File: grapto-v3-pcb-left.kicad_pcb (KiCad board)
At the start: 2 copper layers, 150.1 x 129.9 mm, 62 parts, among them J1 USB_C_Receptacle_USB2.0, J2 USB_C_Receptacle_USB2.0, SW1 SW_Push, SW10 SW_Push, SW11 SW_Push, SW12 SW_Push, SW13 SW_Push, SW14 SW_Push, SW15 SW_Push, SW16 SW_Push, SW17 SW_Push, SW18 SW_Push, SW19 SW_Push, SW2 SW_Push, SW20 SW_Push, SW21 SW_Push, SW22 SW_Push, SW23 SW_Push, SW24 SW_Push, SW25 SW_Push, SW26 SW_Push, SW27 SW_Push, SW28 SW_Push, SW29 SW_Push, SW3 SW_Push, SW30 SW_Push, SW4 SW_Push, SW5 SW_Push, SW6 SW_Push, SW7 SW_Push, SW8 SW_Push, SW9 SW_Push

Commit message: fixed board outline
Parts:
- moved J1 153.8 mm to (215.4, 115.1)
- moved SW25 152.5 mm to (214.7, 145.9), turned to 127.5 degrees
- moved SW30 120.0 mm to (198.5, 131.0), turned to 148 degrees
- moved J2 117.8 mm to (197.4, 115.1)
- moved SW12 113.0 mm to (82.0, 98.0), turned to 180 degrees
- moved SW18 113.0 mm to (82.0, 117.0), turned to 180 degrees
- moved SW24 113.0 mm to (82.0, 151.0), turned to 180 degrees
- moved SW6 113.0 mm to (82.0, 79.0), turned to 180 degrees
- moved D16 108.0 mm to (192.0, 324.6), turned to 180 degrees
- moved D19 108.0 mm to (192.0, 327.6), turned to 180 degrees
- moved D7 108.0 mm to (192.0, 330.5), turned to 180 degrees
- moved D18 97.9 mm to (186.9, 324.6), turned to 180 degrees
- moved D20 97.9 mm to (186.9, 327.6), turned to 180 degrees
- moved D24 97.9 mm to (186.9, 330.5), turned to 180 degrees
- moved D21 87.8 mm to (181.9, 324.6), turned to 180 degrees
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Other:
- outline, holes or cut-outs redrawn

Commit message: Routed signals.
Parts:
- added C1: .1u, Capacitor_SMD:C_0603_1608Metric_Pad1.08x0.95mm_HandSolder, B.Cu at (195.1, 139.0)
- added C10: 32p, Capacitor_SMD:C_0805_2012Metric_Pad1.18x1.45mm_HandSolder, B.Cu at (180.3, 154.0)
- added C11: 32p, Capacitor_SMD:C_0805_2012Metric_Pad1.18x1.45mm_HandSolder, B.Cu at (189.8, 155.2)
- added C12: 1u, Capacitor_SMD:C_0603_1608Metric_Pad1.08x0.95mm_HandSolder, B.Cu at (177.3, 136.1)
- added C2: .1u, Capacitor_SMD:C_0603_1608Metric_Pad1.08x0.95mm_HandSolder, B.Cu at (195.1, 143.8)
- added C3: .1u, Capacitor_SMD:C_0603_1608Metric_Pad1.08x0.95mm_HandSolder, B.Cu at (189.6, 152.5)
- added C4: .1u, Capacitor_SMD:C_0603_1608Metric_Pad1.08x0.95mm_HandSolder, B.Cu at (173.9, 146.2)
- added C5: .1u, Capacitor_SMD:C_0603_1608Metric_Pad1.08x0.95mm_HandSolder, B.Cu at (177.7, 133.9)
- added C6: .1u, Capacitor_SMD:C_0603_1608Metric_Pad1.08x0.95mm_HandSolder, B.Cu at (188.8, 132.3)
- added C7: 1u, Capacitor_SMD:C_0603_1608Metric_Pad1.08x0.95mm_HandSolder, B.Cu at (193.4, 148.8)
- added C8: .1u, Capacitor_SMD:C_0603_1608Metric_Pad1.08x0.95mm_HandSolder, B.Cu at (186.8, 132.2)
- added C9: 1u, Capacitor_SMD:C_0603_1608Metric_Pad1.08x0.95mm_HandSolder, B.Cu at (195.1, 142.2)
- added D31: LED, Diode_SMD:D_0805_2012Metric_Pad1.15x1.40mm_HandSolder, B.Cu at (209.0, 130.7)
- added F1: 200m, Fuse:Fuse_0603_1608Metric_Pad1.05x0.95mm_HandSolder, B.Cu at (192.4, 125.4)
- added R1: 22, Resistor_SMD:R_0603_1608Metric_Pad0.98x0.95mm_HandSolder, B.Cu at (198.8, 127.5)
- added R2: 1.2k, Resistor_SMD:R_0603_1608Metric_Pad0.98x0.95mm_HandSolder, B.Cu at (214.2, 133.4)
- added R3: 1.2k, Resistor_SMD:R_0603_1608Metric_Pad0.98x0.95mm_HandSolder, B.Cu at (213.2, 131.6)
- added R4: 4.7k, Resistor_SMD:R_0603_1608Metric_Pad0.98x0.95mm_HandSolder, B.Cu at (193.5, 151.7)
- added R5: 5.1k, Resistor_SMD:R_0603_1608Metric_Pad0.98x0.95mm_HandSolder, B.Cu at (195.8, 127.5)
- added R6: 5.1k, Resistor_SMD:R_0603_1608Metric_Pad0.98x0.95mm_HandSolder, B.Cu at (200.2, 127.5)
- added R7: 22, Resistor_SMD:R_0603_1608Metric_Pad0.98x0.95mm_HandSolder, B.Cu at (197.2, 127.5)
- added R8: 68, Resistor_SMD:R_0603_1608Metric_Pad0.98x0.95mm_HandSolder, B.Cu at (209.0, 126.2)
- added SW31: SW_SPST, grapto-v3-schematic:Switch_TL3315NF100Q, B.Cu at (199.7, 150.3)
- added TP1: TestPoint, grapto-v3-schematic:TestPoint_S2761-46R, B.Cu at (208.1, 134.8)
- added U1: ATmega32U4-AU, grapto-v3-schematic:QFP-44_10x10_Pitch0.8mm_Hand_solder, B.Cu at (184.5, 142.5)
- added Y1: Crystal_GND24, grapto-v3-schematic:Crystal_ECS-160-20-33-TR3, B.Cu at (184.9, 154.1)
- D1, D10, D11, D12, D13, D14, D15, D16, D17, D18, D19, D2, D20, D21, D22, D23, D24, D25, D26, D27, D28, D29, D3, D30, D4, D5, D6, D7, D8, D9: footprint Diode_SMD:D_SOD-323_HandSoldering -> Diode_SMD:D_SOD-123; moved to B.Cu
- moved D3 286.3 mm to (135.5, 45.0), turned to 270 degrees
- moved D4 285.2 mm to (117.2, 48.8), turned to 270 degrees
- moved D2 278.4 mm to (154.8, 49.2), turned to 270 degrees
- moved D1 277.7 mm to (173.7, 53.6), turned to 270 degrees
- moved D9 264.7 mm to (135.5, 63.6), turned to 270 degrees
- moved D5 264.5 mm to (97.7, 68.7), turned to 270 degrees
- moved D10 263.3 mm to (117.2, 68.0), turned to 270 degrees
- moved D7 259.0 mm to (173.9, 72.1), turned to 270 degrees
- moved D8 256.4 mm to (154.9, 68.2), turned to 270 degrees
- moved D11 253.3 mm to (98.0, 86.8), turned to 270 degrees
- moved D16 249.8 mm to (117.2, 86.3), turned to 270 degrees
- moved D15 247.5 mm to (136.1, 82.0), turned to 270 degrees
- moved D6 247.3 mm to (77.5, 87.2), turned to 270 degrees
- moved D14 244.3 mm to (154.9, 87.2), turned to 270 degrees
- moved D13 239.3 mm to (173.9, 91.2), turned to 270 degrees
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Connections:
- net col0 renamed /Sheet6188018D/col0
- net col1 renamed /Sheet6188018D/col1
- net col2 renamed /Sheet6188018D/col2
- net col3 renamed /Sheet6188018D/col3
- net col4 renamed /Sheet6188018D/col4
- net col5 renamed /Sheet6188018D/col5
- net row0 renamed /Sheet6188018D/row0
- net row1 renamed /Sheet6188018D/row1
- net row2 renamed /Sheet6188018D/row2
- net row3 renamed /Sheet6188018D/row3
- net row4 renamed /Sheet6188018D/row4
- J1 pad A12: Net-(J1-PadA1) -> 0V
- J1 pad A4: Net-(J1-PadA4) -> VBUS
- J1 pad A6: Net-(J1-PadA6) -> /Sheet61884E9A/SCL
- J1 pad A7: Net-(J1-PadA7) -> /Sheet61884E9A/SDA
- J1 pad B12: Net-(J1-PadA1) -> 0V
- J1 pad B4: Net-(J1-PadA4) -> VBUS
- J1 pad B6: Net-(J1-PadB6) -> /Sheet61884E9A/SCL
- J1 pad B7: Net-(J1-PadB7) -> /Sheet61884E9A/SDA
- J1 pad S1: Net-(J1-PadS1) -> 0V
- J2 pad A12: Net-(J2-PadA1) -> 0V
- J2 pad A4: Net-(J2-PadA4) -> VBUS
- J2 pad A6: Net-(J2-PadA6) -> /Sheet61884E9A/USB_FULL_P1
- J2 pad A7: Net-(J2-PadA7) -> /Sheet61884E9A/USB_FULL_N1
- J2 pad B12: Net-(J2-PadA1) -> 0V
- J2 pad B4: Net-(J2-PadA4) -> VBUS
- J2 pad B6: Net-(J2-PadB6) -> /Sheet61884E9A/USB_FULL_P1
- J2 pad B7: Net-(J2-PadB7) -> /Sheet61884E9A/USB_FULL_N1
- J2 pad S1: Net-(J2-PadS1) -> 0V
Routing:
- net /Sheet6188018D/row0: track 0.00 -> 283.3 mm
- net /Sheet6188018D/row1: track 0.00 -> 264.3 mm
- net /Sheet6188018D/row3: track 0.00 -> 231.0 mm, vias 0 -> 4
- net /Sheet6188018D/row2: track 0.00 -> 230.2 mm
- net /Sheet6188018D/row4: track 0.00 -> 215.4 mm, vias 0 -> 6
- net /Sheet6188018D/col0: track 0.00 -> 184.4 mm, vias 0 -> 6
- net /Sheet6188018D/col5: track 0.00 -> 177.2 mm, vias 0 -> 8
- net /Sheet6188018D/col3: track 0.00 -> 175.5 mm, vias 0 -> 8
- net /Sheet6188018D/col4: track 0.00 -> 163.7 mm, vias 0 -> 8
- net /Sheet6188018D/col2: track 0.00 -> 155.0 mm, vias 0 -> 10
- net 5V: track 0.00 -> 138.2 mm
- net /Sheet6188018D/col1: track 0.00 -> 128.9 mm, vias 0 -> 10
- net /Sheet61884E9A/SDA: track 0.00 -> 80.0 mm, vias 0 -> 2
- net /Sheet61884E9A/SCL: track 0.00 -> 73.5 mm, vias 0 -> 2
- net (no net): track 0.00 -> 64.2 mm, vias 0 -> 52
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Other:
- net class Default: trace_width 0.25 -> 0.15
- net class PWR added: clearance 0.2, trace_width 0.4, via_dia 0.8, via_drill 0.4
- rule trace_min: 0.2 -> 0.15

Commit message: First layout done
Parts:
- moved D30 7.84 mm to (181.2, 131.4), turned to 270 degrees
- moved R3 3.63 mm to (213.4, 135.2)
- moved R2 1.74 mm to (212.4, 133.3)
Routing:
- net (no net): track 64.2 -> 0.00 mm, vias 52 -> 0
- net 0V: track 31.4 -> 89.5 mm, vias 0 -> 27
- net VBUS: track 18.9 -> 48.8 mm, vias 0 -> 2
- net /Sheet6188018D/col5: track 177.2 -> 169.2 mm, vias 8 -> 6
- net Net-(D30-Pad1): track 5.42 -> 12.8 mm
- net /Sheet61884E9A/SCL: track 73.5 -> 78.1 mm, vias 2 -> 4
- net Net-(D29-Pad1): track 0.00 -> 3.62 mm
- net /Sheet61884E9A/XTAL2: track 9.90 -> 11.8 mm
- net /Sheet61884E9A/SDA: track 80.0 -> 81.6 mm, vias 2 -> 0
- net /Sheet6188018D/col0: track 184.4 -> 186.0 mm, vias 6 -> 8
- net 5V: track 138.2 -> 137.1 mm
- net /Sheet61884E9A/USB_FULL_N1: track 8.22 -> 8.94 mm
- added copper zone on F.Cu, net 0V

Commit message: Update silkscreen
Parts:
- added REF**: KiCad-Logo_8mm_SilkScreen, Symbol:KiCad-Logo_8mm_SilkScreen, B.Cu at (127.7, 145.6)
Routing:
- net /Sheet6188018D/col1: track 128.8 -> 134.0 mm
- net Net-(D14-Pad1): track 0.00 -> 3.54 mm
- net 0V: track 89.5 -> 92.2 mm, vias 27 -> 29
- net /Sheet6188018D/row2: track 230.2 -> 230.8 mm
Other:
- board text added: "Grapto v3 left, Herman Lundkvist"

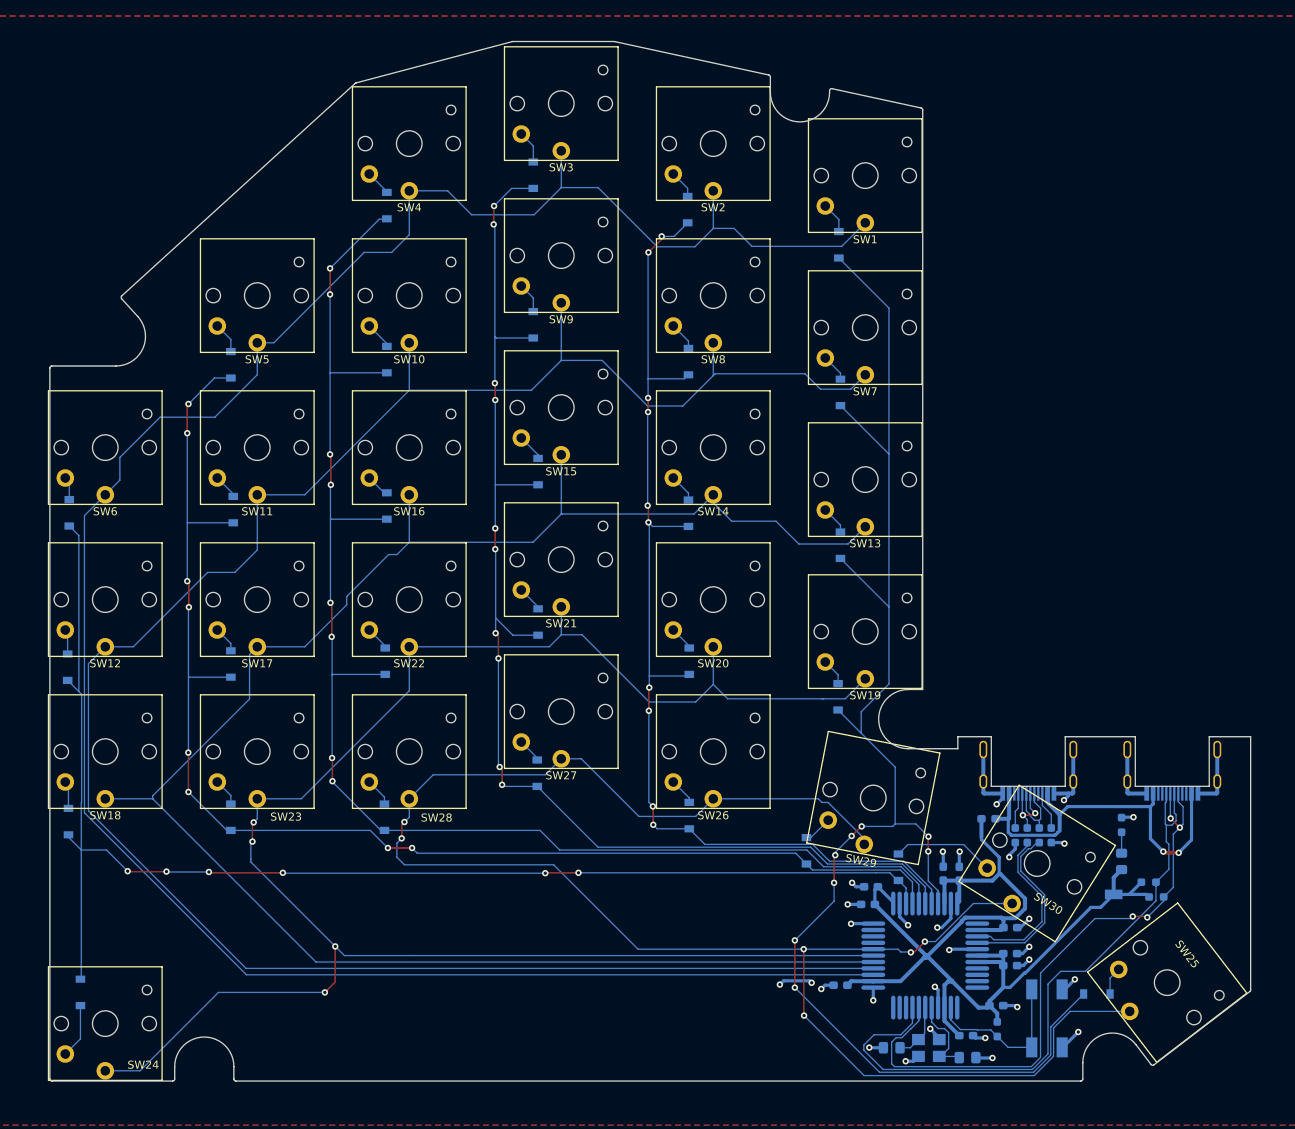
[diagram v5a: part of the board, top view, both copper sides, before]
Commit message: Update switch footprint.
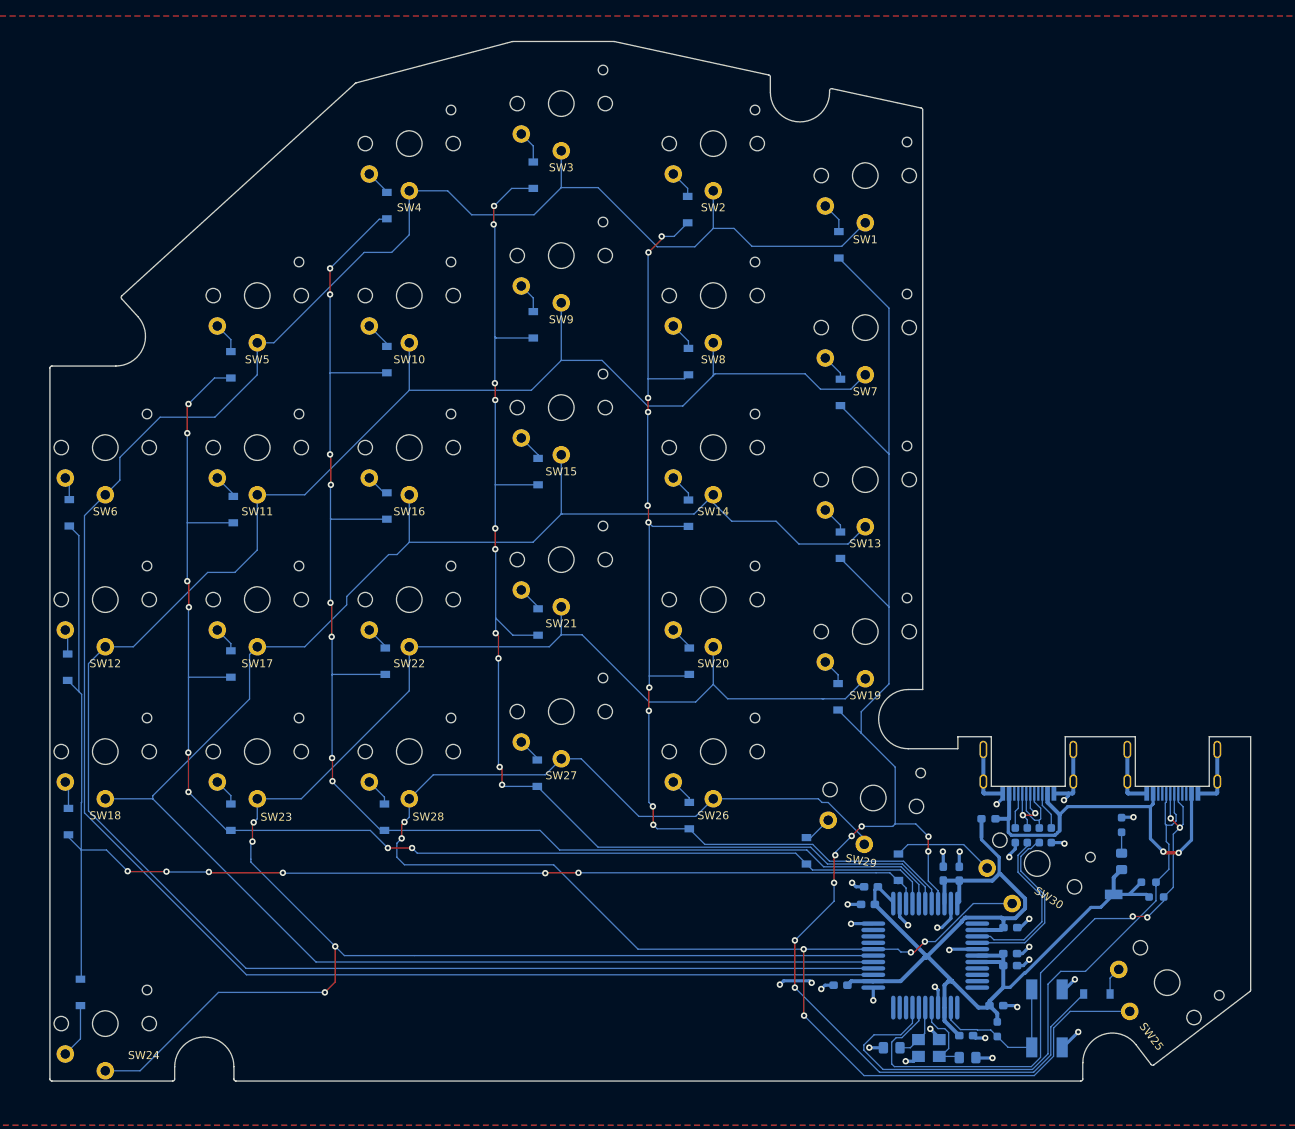
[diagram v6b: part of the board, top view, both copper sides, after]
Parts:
- removed REF**: KiCad-Logo_8mm_SilkScreen, Symbol:KiCad-Logo_8mm_SilkScreen
- SW1, SW10, SW11, SW12, SW13, SW14, SW15, SW16, SW17, SW18, SW19, SW2, SW20, SW21, SW22, SW23, SW24, SW25, SW26, SW27, SW28, SW29, SW3, SW30, SW4, SW5, SW6, SW7, SW8, SW9: footprint kaihl_choc:SW_Kailh_Choc_V1 -> grapto-v3-schematic:SW_Kailh_Choc_V1
